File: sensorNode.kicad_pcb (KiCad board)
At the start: 2 copper layers, 57 x 32 mm, 20 parts, among them P1 PIR, P2 PRGM, P3 Serial I/O, SW1 Reset, U1 ESP-12, U2 DS18B20, U3 ISL29035

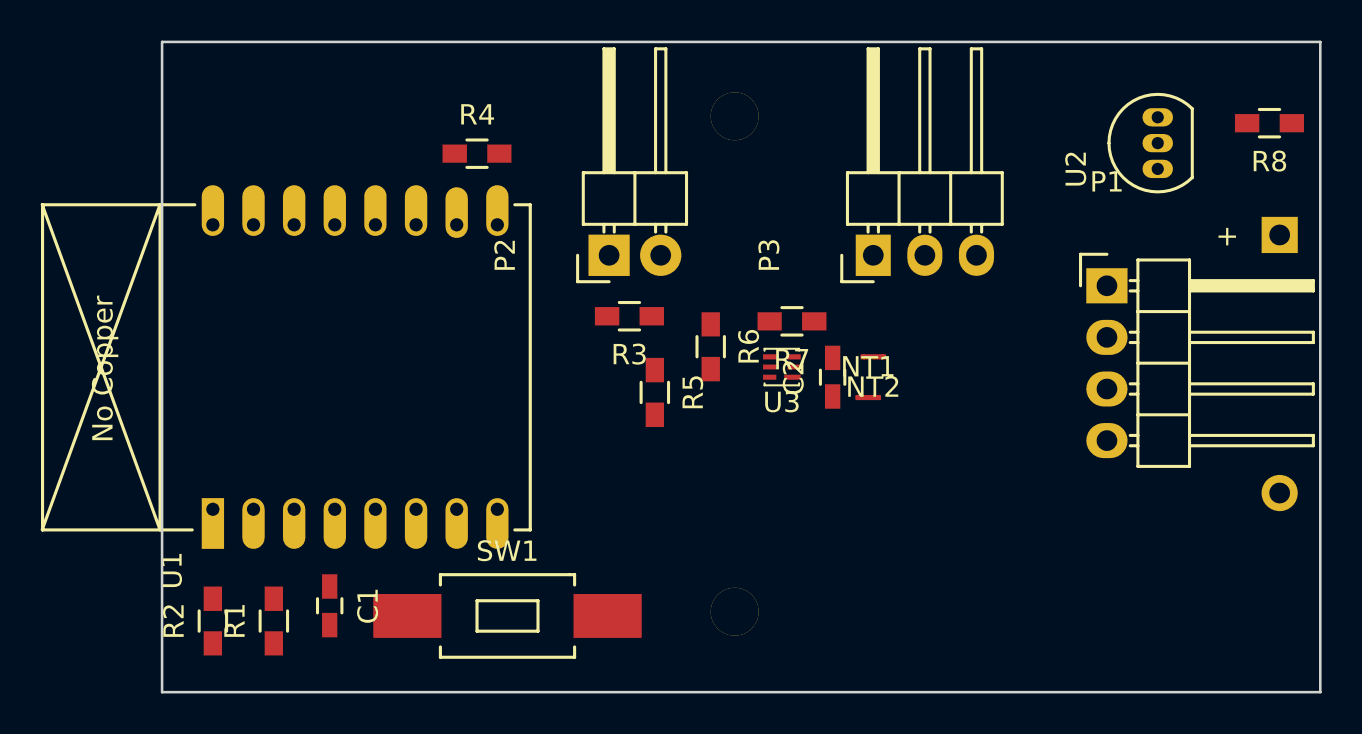
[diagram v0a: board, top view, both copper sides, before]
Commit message: Routing complete
On branch newPCB
modified:   sensorNode.kicad_pcb
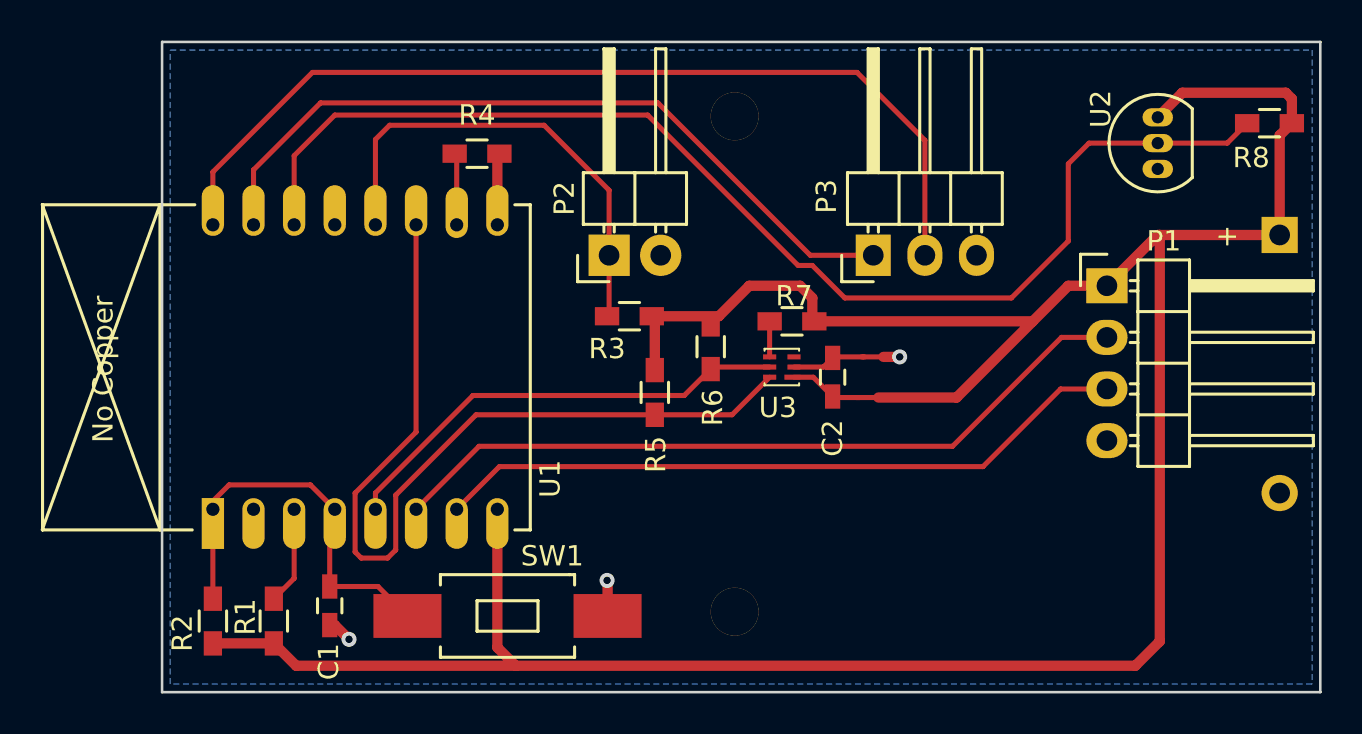
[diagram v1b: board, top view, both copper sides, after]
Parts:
- renumbered NT2 to ?, NT1 to ?
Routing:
- net VCC: track 0.00 -> 136.3 mm
- net Net-(R8-Pad2): track 0.00 -> 60.6 mm
- net Net-(P3-Pad2): track 0.00 -> 46.7 mm
- net /I2C_SDA: track 0.00 -> 43.1 mm
- net Net-(P3-Pad1): track 0.00 -> 37.7 mm
- net /PIR-Repeat: track 0.00 -> 37.5 mm
- net /PIR-Motion: track 0.00 -> 34.5 mm
- net Net-(P2-Pad1): track 0.00 -> 23.6 mm
- net /I2C_SCL: track 0.00 -> 22.8 mm
- net Net-(C1-Pad1): track 0.00 -> 19.8 mm
- net GND: track 0.00 -> 7.44 mm, vias 0 -> 3
- net Net-(R1-Pad2): track 0.00 -> 4.81 mm
- net /SMD_GND: track 0.00 -> 3.61 mm
- net /SMD_VDD: track 0.00 -> 3.56 mm
- net Net-(R4-Pad1): track 0.00 -> 3.54 mm
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- added copper zone on B.Cu, net GND
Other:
- net class Default: via_dia 0.6 -> 0.7366; via_drill 0.4 -> 0.381
- net class Minimum added: clearance 0.1524, trace_width 0.1524, via_dia 0.6858, via_drill 0.3302
- net class PWR added: clearance 0.2, trace_width 0.508, via_dia 0.7366, via_drill 0.381
- rule trace_min: 0.2 -> 0.1524
- rule via_min_drill: 0.3 -> 0.3302
- rule via_min_size: 0.4 -> 0.3302

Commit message: Add labels on silkscreen
On branch newPCB
modified:   sensorNode.kicad_pcb
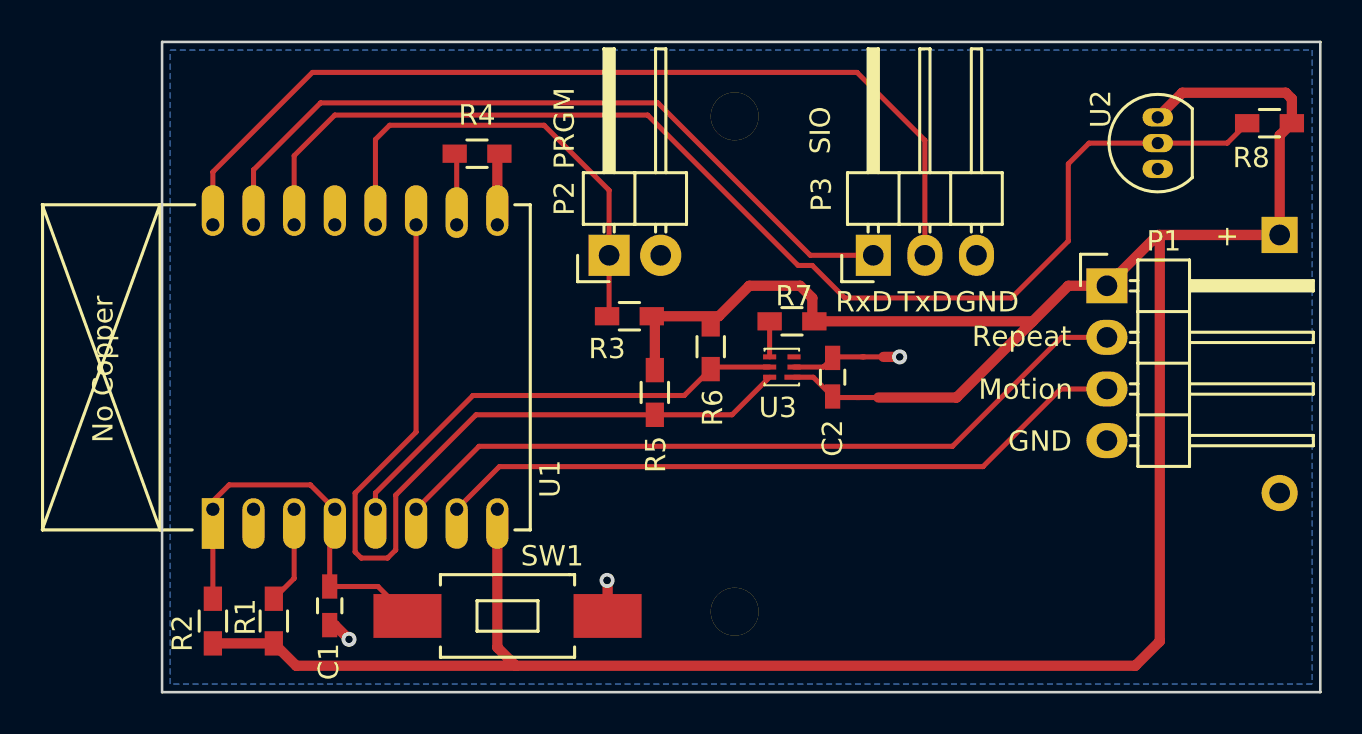
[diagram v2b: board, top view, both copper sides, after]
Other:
- board text added: "GND"
- board text added: "Motion"
- board text added: "PRGM"
- board text added: "Repeat"
- board text added: "RxD"
- board text added: "SIO"
- board text added: "TxD"
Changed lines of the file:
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@@
-(kicad_pcb (version 4) (host pcbnew 0.201505262310+5684~23~ubuntu14.04.1-product)
+(kicad_pcb (version 4) (host pcbnew 0.201506292248+5841~23~ubuntu14.04.1-product)
   (general
     (links 43)
     (no_connects 0)
-    (area 44.936499 90.436499 102.063501 122.563501)
+    (area 33.499499 84.499499 110.000501 133.000501)
     (thickness 1.6)
-    (drawings 10)
+    (drawings 18)
     (tracks 115)
     (zones 0)
@@
     (pad_to_mask_clearance 0.05)
     (aux_axis_origin 0 0)
-    (visible_elements FFFFFF3F)
+    (visible_elements FFFEFF3F)
     (pcbplotparams
       (layerselection 0x00030_80000001)
@@
     (descr "Through hole pin header")
     (tags "pin header")
-    (fp_text reference P3 (at 2.9 -2.3 90) (layer F.SilkS)
+    (fp_text reference P3 (at 3 -2.55 90) (layer F.SilkS)
       (effects (font (size 1 1) (thickness 0.15)))
     )
@@
       (net 4 /SMD_VDD))
   )
+  (gr_text GND (at 88.2 110.15) (layer F.SilkS)
+    (effects (font (size 1 1) (thickness 0.15)))
+  )
+  (gr_text SIO (at 77.4 94.85 90) (layer F.SilkS)
+    (effects (font (size 1 1) (thickness 0.15)))
+  )
+  (gr_text PRGM (at 64.8 94.75 90) (layer F.SilkS)
+    (effects (font (size 1 1) (thickness 0.15)))
+  )
+  (gr_text Repeat (at 87.3 105) (layer F.SilkS)
+    (effects (font (size 1 1) (thickness 0.15)))
+  )
+  (gr_text Motion (at 87.5 107.6) (layer F.SilkS)
+    (effects (font (size 1 1) (thickness 0.15)))
+  )
+  (gr_text GND (at 85.6 103.3) (layer F.SilkS)
+    (effects (font (size 1 1) (thickness 0.15)))
+  )
+  (gr_text RxD (at 79.55 103.3) (layer F.SilkS)
+    (effects (font (size 1 1) (thickness 0.15)))
+  )
+  (gr_text TxD (at 82.55 103.3) (layer F.SilkS)
+    (effects (font (size 1 1) (thickness 0.15)))
+  )
   (gr_line (start 73.5 84.5) (end 73.5 133) (angle 90) (layer F.Fab) (width 0.001))
   (gr_line (start 33.5 106.5) (end 110 106.5) (angle 90) (layer F.Fab) (width 0.001))
@@
   (segment (start 66.925 118.75) (end 66.925 117.025) (width 0.508) (layer F.Cu) (net 2))
   (segment (start 66.9 117) (end 66.9 117.1) (width 0.508) (layer B.Cu) (net 2))
-  (via (at 66.9 117) (size 0.7366) (layers F.Cu B.Cu) (net 2))
+  (via (at 66.9 117) (size 0.7366) (drill 0.381) (layers F.Cu B.Cu) (net 2))
   (segment (start 66.925 117.025) (end 66.9 117) (width 0.508) (layer F.Cu) (net 2))
   (segment (start 53.25 119.2) (end 53.5 119.2) (width 0.508) (layer F.Cu) (net 2))

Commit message: Add part details for BOM
On branch newPCB
modified:   sensorNode.kicad_pcb
modified:   sensorNode.net
modified:   sensorNode.sch
modified:   sensorNode.xml
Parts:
- moved NT2 2.01 mm to (80.0, 106.0), turned to 0 degrees
- moved NT1 2.00 mm to (79.8, 108.0), turned to 180 degrees
- gave numbers to parts that had none: 2
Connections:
- NT1 pad 1: /SMD_GND -> VCC
- NT1 pad 2: GND -> /SMD_VDD
- NT2 pad 1: VCC -> /SMD_GND
- NT2 pad 2: /SMD_VDD -> GND
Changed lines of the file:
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@@
-(kicad_pcb (version 4) (host pcbnew 0.201506292248+5841~23~ubuntu14.04.1-product)
+(kicad_pcb (version 4) (host pcbnew 0.201507310902+6023~28~ubuntu14.04.1-product)
   (general
     (links 43)
     (no_connects 0)
-    (area 33.499499 84.499499 110.000501 133.000501)
+    (area 44.936499 90.436499 102.063501 122.563501)
     (thickness 1.6)
     (drawings 18)
-    (tracks 115)
+    (tracks 117)
     (zones 0)
     (modules 20)
@@
   )
   (module sensorNode:NetTie-0.25mm_Connected_SMD (layer F.Cu)
-    (at 80 106)
+    (at 79.81 107.99 180)
     (descr "Just a \"Net tie\" as an more or less elegant way to connect two different nets without disturbing ERC and DRC.")
     (tags "Just a \"Net tie\" as an more or less elegant way to connect two different nets without disturbing ERC and DRC.")
-    (fp_text reference "" (at 3 0.1) (layer F.SilkS)
+    (fp_text reference NT1 (at -0.6 -1.2 180) (layer F.SilkS) hide
+      (effects (font (size 1 1) (thickness 0.15)))
+    )
+    (fp_text value Net-Tie-2 (at 0 -1.5 180) (layer F.Fab)
+      (effects (font (size 1 1) (thickness 0.15)))
+    )
+    (fp_line (start 0.5 0) (end -0.5 0) (layer F.Cu) (width 0.25))
+    (pad 1 smd rect (at -0.5 0 180) (size 0.25 0.25) (layers F.Cu F.Paste F.Mask)
+      (net 1 VCC))
+    (pad 2 smd rect (at 0.5 0 180) (size 0.25 0.25) (layers F.Cu F.Paste F.Mask)
+      (net 4 /SMD_VDD))
+  )
+  (module sensorNode:NetTie-0.25mm_Connected_SMD (layer F.Cu)
+    (at 79.99 106)
+    (descr "Just a \"Net tie\" as an more or less elegant way to connect two different nets without disturbing ERC and DRC.")
+    (tags "Just a \"Net tie\" as an more or less elegant way to connect two different nets without disturbing ERC and DRC.")
+    (fp_text reference NT2 (at 0 1.5) (layer F.SilkS) hide
       (effects (font (size 1 1) (thickness 0.15)))
     )
@@
     (pad 2 smd rect (at 0.5 0) (size 0.25 0.25) (layers F.Cu F.Paste F.Mask)
       (net 2 GND))
-  )
-  (module sensorNode:NetTie-0.25mm_Connected_SMD (layer F.Cu)
-    (at 79.75 108 180)
-    (descr "Just a \"Net tie\" as an more or less elegant way to connect two different nets without disturbing ERC and DRC.")
-    (tags "Just a \"Net tie\" as an more or less elegant way to connect two different nets without disturbing ERC and DRC.")
-    (fp_text reference "" (at 0 1.5 180) (layer F.SilkS)
-      (effects (font (size 1 1) (thickness 0.15)))
-    )
-    (fp_text value Net-Tie-2 (at 0 -1.5 180) (layer F.Fab)
-      (effects (font (size 1 1) (thickness 0.15)))
-    )
-    (fp_line (start 0.5 0) (end -0.5 0) (layer F.Cu) (width 0.25))
-    (pad 1 smd rect (at -0.5 0 180) (size 0.25 0.25) (layers F.Cu F.Paste F.Mask)
-      (net 1 VCC))
-    (pad 2 smd rect (at 0.5 0 180) (size 0.25 0.25) (layers F.Cu F.Paste F.Mask)
-      (net 4 /SMD_VDD))
   )
   (gr_text GND (at 88.2 110.15) (layer F.SilkS)
@@
   (gr_line (start 102 90.5) (end 45 90.5) (angle 90) (layer Edge.Cuts) (width 0.127))
   (gr_line (start 102 122.5) (end 102 90.5) (angle 90) (layer Edge.Cuts) (width 0.127))
-  (segment (start 80.25 108) (end 84.1 108) (width 0.508) (layer F.Cu) (net 1))
-  (segment (start 84.1 108) (end 87.85 104.25) (width 0.508) (layer F.Cu) (net 1))
   (segment (start 61.5 113.5) (end 61.5 120.3) (width 0.508) (layer F.Cu) (net 1))
   (segment (start 61.5 120.3) (end 62.4 121.2) (width 0.508) (layer F.Cu) (net 1))
@@
   (segment (start 94 100) (end 91.5 102.5) (width 0.508) (layer F.Cu) (net 1))
   (segment (start 91.5 102.5) (end 89.6 102.5) (width 0.508) (layer F.Cu) (net 1))
-  (segment (start 89.6 102.5) (end 87.85 104.25) (width 0.508) (layer F.Cu) (net 1))
   (segment (start 87.85 104.25) (end 77.1 104.25) (width 0.508) (layer F.Cu) (net 1))
   (segment (start 77.1 104.25) (end 77 104.15) (width 0.508) (layer F.Cu) (net 1))
@@
   (segment (start 100.3 93) (end 95.21 93) (width 0.508) (layer F.Cu) (net 1))
   (segment (start 95.21 93) (end 94 94.21) (width 0.508) (layer F.Cu) (net 1))
+  (segment (start 84.1 108) (end 87.85 104.25) (width 0.508) (layer F.Cu) (net 1))
+  (segment (start 89.6 102.5) (end 87.85 104.25) (width 0.508) (layer F.Cu) (net 1))
+  (segment (start 80.25 108) (end 84.1 108) (width 0.508) (layer F.Cu) (net 1))
   (segment (start 61.5 99.5) (end 61.5 96.1) (width 0.508) (layer F.Cu) (net 2))
   (segment (start 61.5 96.1) (end 61.6 96) (width 0.508) (layer F.Cu) (net 2))
@@
   (segment (start 55.625 117.3) (end 57.075 118.75) (width 0.25) (layer F.Cu) (net 3))
   (segment (start 47.5 113.5) (end 47.5 117.9) (width 0.25) (layer F.Cu) (net 3))
-  (segment (start 79.25 108) (end 78.05 108) (width 0.25) (layer F.Cu) (net 4))
+  (segment (start 78.04 107.99) (end 78 107.95) (width 0.25) (layer F.Cu) (net 4))
+  (segment (start 79.31 107.99) (end 78.04 107.99) (width 0.25) (layer F.Cu) (net 4))
   (segment (start 78.05 108) (end 77.05 107) (width 0.25) (layer F.Cu) (net 4))
   (segment (start 77.05 107) (end 76.1 107) (width 0.25) (layer F.Cu) (net 4))
-  (segment (start 79.5 106) (end 78.05 106) (width 0.25) (layer F.Cu) (net 5))
+  (segment (start 79.49 106) (end 78.05 106) (width 0.25) (layer F.Cu) (net 5))
+  (segment (start 78.05 106) (end 78 106.05) (width 0.25) (layer F.Cu) (net 5))
   (segment (start 78.05 106) (end 77.55 106.5) (width 0.25) (layer F.Cu) (net 5))
   (segment (start 77.55 106.5) (end 76.1 106.5) (width 0.25) (layer F.Cu) (net 5))

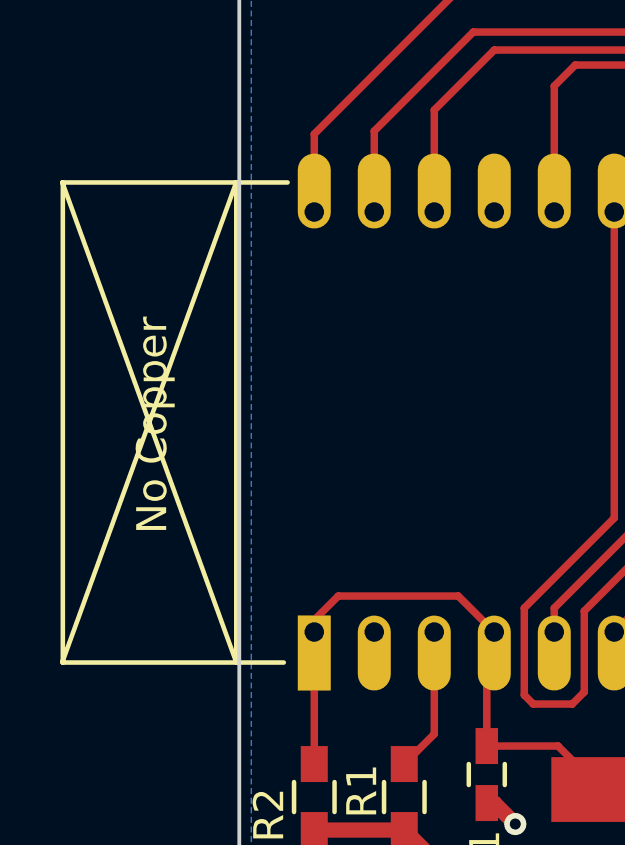
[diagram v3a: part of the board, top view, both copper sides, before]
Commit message: Use ESP-12 footprint with smaller silkscreen
On branch newPCB
modified:   sensorNode.kicad_pcb
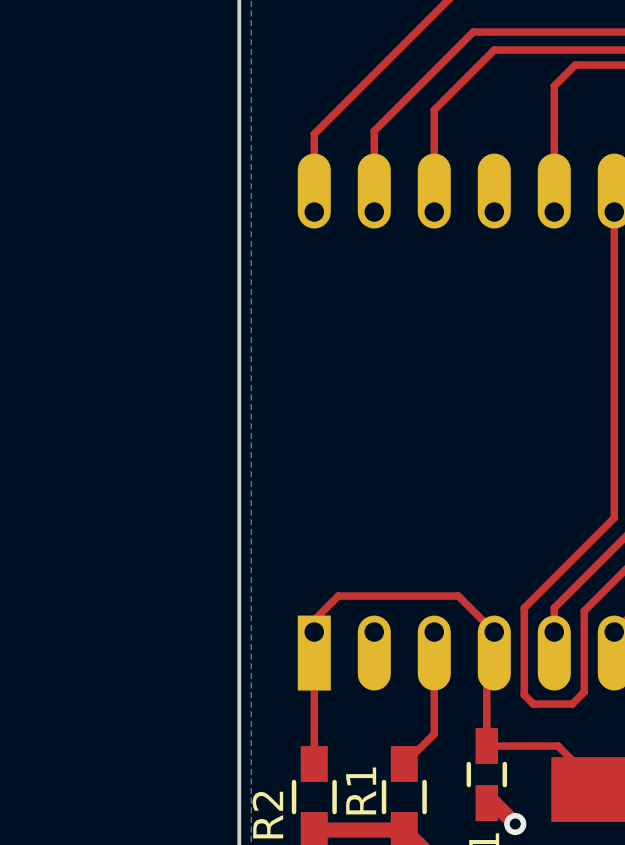
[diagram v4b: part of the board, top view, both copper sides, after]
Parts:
- U1: footprint ESP8266:ESP-12 -> ESP-12

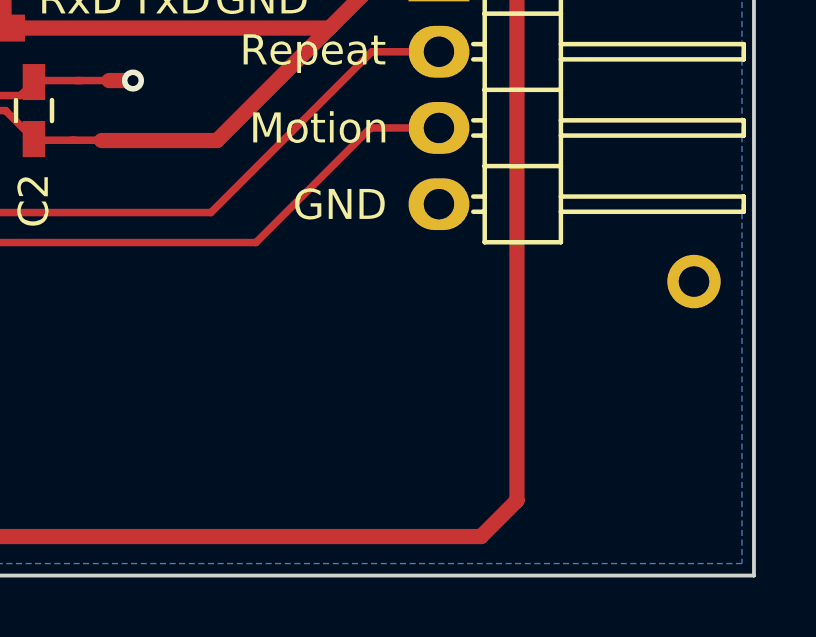
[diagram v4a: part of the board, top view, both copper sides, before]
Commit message: Use batter holder with outline on comments layer
If outline was left on the silkscreen, the board size would
have to be larger.

On branch newPCB
modified:   sensorNode.kicad_pcb
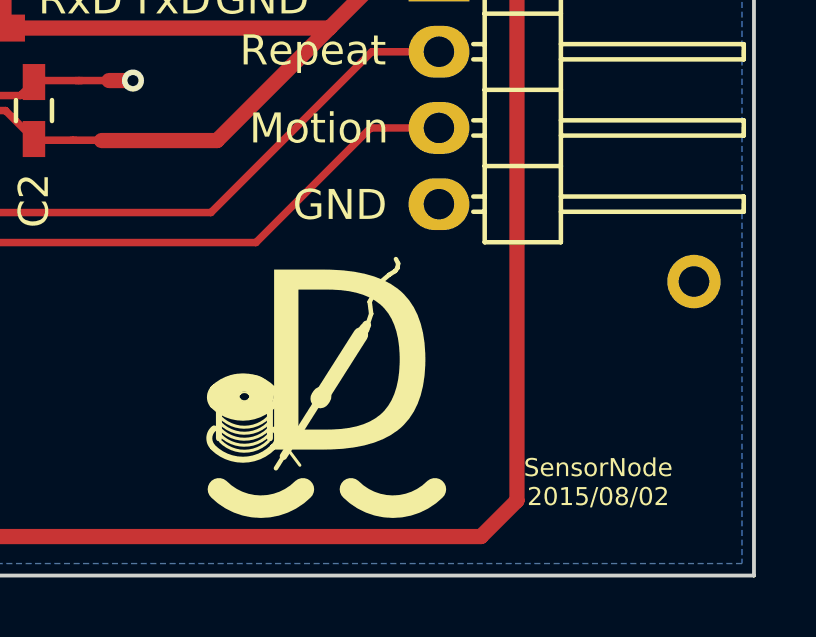
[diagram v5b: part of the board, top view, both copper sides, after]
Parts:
- added ?: RockingDLogo_9x7, rockingDLogos:RockingDLogo_9x7, F.Cu at (87.7, 120.5)
- added ?: RockingDLogo_9x7, rockingDLogos:RockingDLogo_9x7, B.Cu at (53.9, 101.4)
- BT1: footprint Battery_Holders:BA2AAPC -> BA2AAPC
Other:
- board text added: "SensorNode 2015/08/02"
- board text added: "SensorNode Copyright 2015 J. Dunmire All Rights Reserved jerry@dunmire.org"

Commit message: Rotate logo on bottom
On branch newPCB
new file:   CAM/.gitignore
modified:   sensorNode.kicad_pcb
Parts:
- moved ? 9.66 mm to (54.5, 111.1), turned to 180 degrees
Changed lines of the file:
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@@
     (pcbplotparams
       (layerselection 0x010f0_80000001)
-      (usegerberextensions false)
+      (usegerberextensions true)
       (excludeedgelayer true)
       (linewidth 0.100000)
@@
   )
   (module rockingDLogos:RockingDLogo_9x7 (layer B.Cu)
-    (at 53.87 101.43)
+    (at 54.47 111.07 180)
     (descr "RockingDLabs-logo, 9x7mm, Silkscreen,")
     (tags "RockigDLabs-Logo, 9x7mm, Silkscreen,")
-    (fp_text reference "" (at 0 10) (layer B.SilkS) hide
+    (fp_text reference "" (at 0 10 180) (layer B.SilkS) hide
       (effects (font (size 1 1) (thickness 0.15)) (justify mirror))
     )
-    (fp_text value RockingDLogo_9x7 (at 0 11.75) (layer B.Fab)
+    (fp_text value RockingDLogo_9x7 (at 0 11.75 180) (layer B.Fab)
       (effects (font (size 1 1) (thickness 0.15)) (justify mirror))
     )
@@
     (fp_arc (start 2.225 2.325) (end 3.625 0.925) (angle -90) (layer B.SilkS) (width 0.75))
     (fp_arc (start -2.175 2.325) (end -0.775 0.925) (angle -90) (layer B.SilkS) (width 0.75))
-    (fp_text user D (at 0.625 5.025) (layer B.SilkS)
+    (fp_text user D (at 0.625 5.025 180) (layer B.SilkS)
       (effects (font (size 6 6) (thickness 0.75)) (justify mirror))
     )
